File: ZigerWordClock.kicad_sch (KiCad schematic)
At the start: 61 parts, among them J1 SAO 1.69bis, U1 BH1750, U10 BTF-5V-060L-B_SK9822_LED_Stri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, U11 BTF-5V-060L-B_SK9822_LED_Stri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, U12 BTF-5V-060L-B_SK9822_LED_Stri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, U13 BTF-5V-060L-B_SK9822_LED_Stri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, U14 BTF-5V-060L-B_SK9822_LED_Stri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, U15 BTF-5V-060L-B_SK9822_LED_Stri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, U16 BTF-5V-060L-B_SK9822_LED_Stri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, U17 BTF-5V-060L-B_SK9822_LED_Stri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, U18 BTF-5V-060L-B_SK9822_LED_Stri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, U19 BTF-5V-060L-B_SK9822_LED_Stri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, U2 LILYGO(R)_TTGO_T8_ESP32-S2_V1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, U20 IR-Module_38KHz, U3 BTF-5V-060L-B_SK9822_LED_Stri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, U4 LevelShifter, U5 BTF-5V-060L-B_SK9822_LED_Stri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, U6 BTF-5V-060L-B_SK9822_LED_Stri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, U7 BTF-5V-060L-B_SK9822_LED_Stri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, U8 BTF-5V-060L-B_SK9822_LED_Stri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, U9 BTF-5V-060L-B_SK9822_LED_Stri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

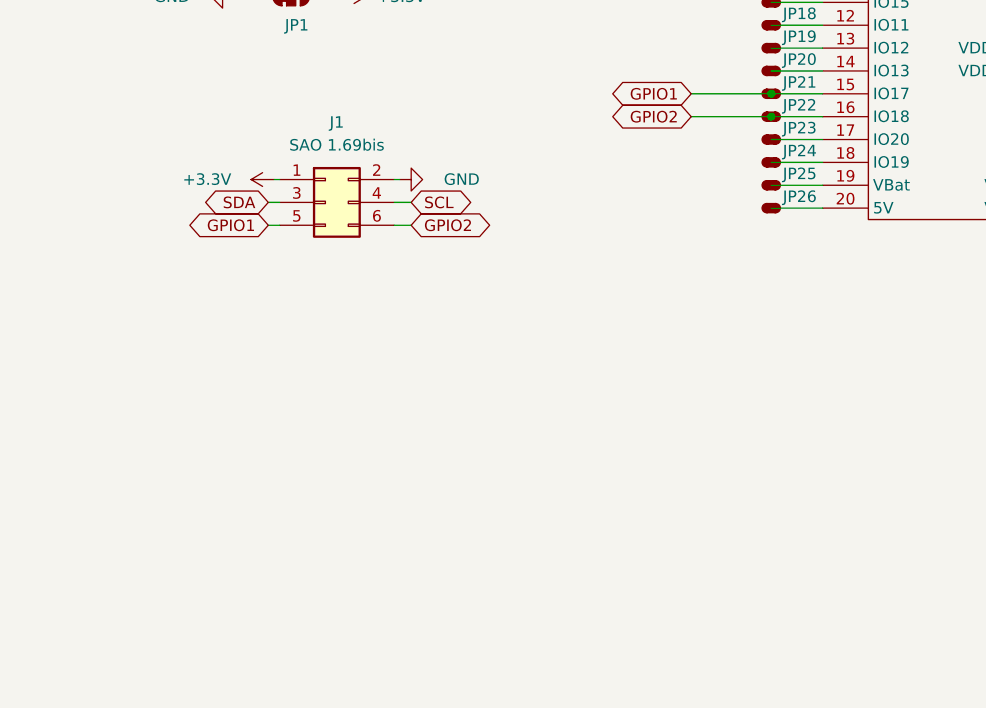
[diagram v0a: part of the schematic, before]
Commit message: Pin labels added
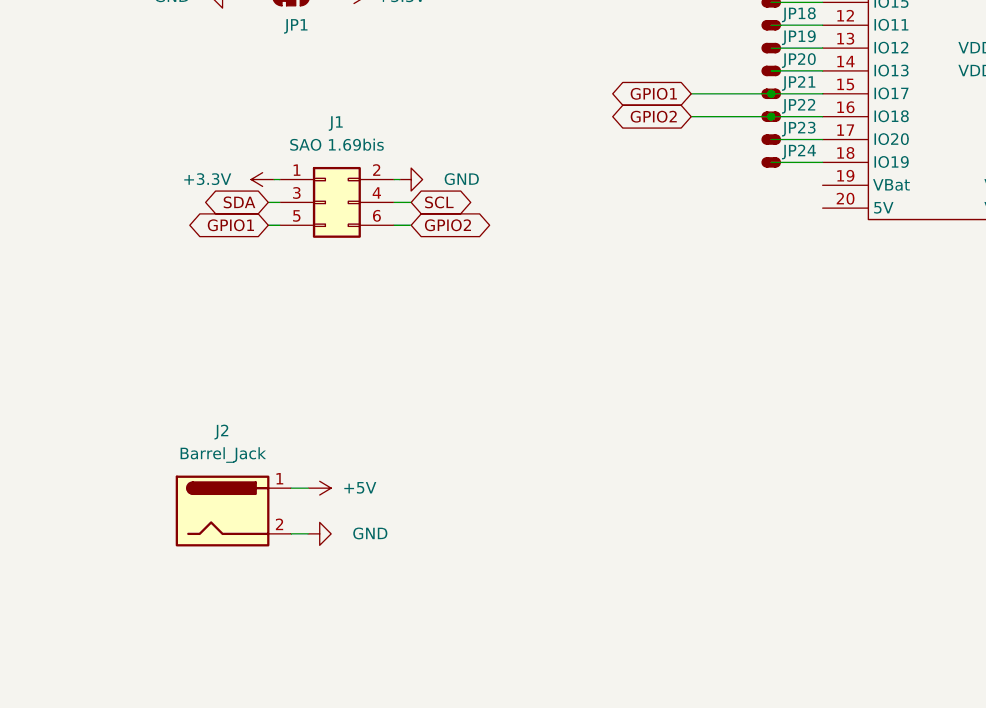
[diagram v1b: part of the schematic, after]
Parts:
- removed JP25, JP26: Pad, WordClock Footprint Library:Pad, symbol WordClock Symbol Library:Pad
- added J2: Barrel_Jack, Connector_PinHeader_2.54mm:PinHeader_1x02_P2.54mm_Vertical, symbol Connector:Barrel_Jack
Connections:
- net +5V: now also J2.1
- net GND: now also J2.2
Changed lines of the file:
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@@
     (stroke (width 0) (type default) (color 0 0 0 0))
   )
-  (wire (pts (xy 154.305 125.095) (xy 160.02 125.095))
-    (stroke (width 0) (type default) (color 0 0 0 0))
-  )
   (wire (pts (xy 165.1 203.2) (xy 168.91 203.2))
     (stroke (width 0) (type default) (color 0 0 0 0))
@@
     (stroke (width 0) (type default) (color 0 0 0 0))
   )
+  (wire (pts (xy 102.87 163.83) (xy 100.965 163.83))
+    (stroke (width 0) (type default) (color 0 0 0 0))
+  )
   (wire (pts (xy 322.58 190.5) (xy 331.47 190.5))
     (stroke (width 0) (type default) (color 0 0 0 0))
@@
     (stroke (width 0) (type default) (color 0 0 0 0))
   )
+  (wire (pts (xy 102.87 158.75) (xy 100.965 158.75))
+    (stroke (width 0) (type default) (color 0 0 0 0))
+  )
   (wire (pts (xy 154.305 112.395) (xy 160.02 112.395))
     (stroke (width 0) (type default) (color 0 0 0 0))
@@
     (stroke (width 0) (type default) (color 0 0 0 0))
   )
-  (wire (pts (xy 154.305 127.635) (xy 160.02 127.635))
-    (stroke (width 0) (type default) (color 0 0 0 0))
-  )
   (wire (pts (xy 320.04 193.04) (xy 331.47 193.04))
     (stroke (width 0) (type default) (color 0 0 0 0))
@@
   (symbol (lib_id "power:GND") (at 189.23 114.935 90) (mirror x) (unit 1)
     (in_bom yes) (on_board yes) (fields_autoplaced)
-    (property "Reference" "#PWR?" (id 0) (at 195.58 114.935 0)
+    (property "Reference" "#PWR0185" (id 0) (at 195.58 114.935 0)
       (effects (font (size 1.27 1.27)) hide)
     )
@@
     (pin "GND_2")
   )
+  (symbol (lib_id "Connector:Barrel_Jack") (at 93.345 161.29 0) (unit 1)
+    (in_bom yes) (on_board yes) (fields_autoplaced)
+    (property "Reference" "J2" (id 0) (at 93.345 152.4 0))
+    (property "Value" "Barrel_Jack" (id 1) (at 93.345 154.94 0))
+    (property "Footprint" "Connector_PinHeader_2.54mm:PinHeader_1x02_P2.54mm_Vertical" (id 2) (at 94.615 162.306 0)
+      (effects (font (size 1.27 1.27)) hide)
+    )
+    (property "Datasheet" "~" (id 3) (at 94.615 162.306 0)
+      (effects (font (size 1.27 1.27)) hide)
+    )
+    (pin "1")
+    (pin "2")
+  )
   (symbol (lib_id "power:+5V") (at 331.47 73.66 90) (unit 1)
     (in_bom yes) (on_board yes) (fields_autoplaced)
@@
     (pin "1")
   )
+  (symbol (lib_id "power:GND") (at 102.87 163.83 90) (unit 1)
+    (in_bom yes) (on_board yes)
+    (property "Reference" "#PWR0183" (id 0) (at 109.22 163.83 0)
+      (effects (font (size 1.27 1.27)) hide)
+    )
+    (property "Value" "GND" (id 1) (at 111.76 163.83 90)
+      (effects (font (size 1.27 1.27)) (justify left))
+    )
+    (property "Footprint" "" (id 2) (at 102.87 163.83 0)
+      (effects (font (size 1.27 1.27)) hide)
+    )
+    (property "Datasheet" "" (id 3) (at 102.87 163.83 0)
+      (effects (font (size 1.27 1.27)) hide)
+    )
+    (pin "1")
+  )
   (symbol (lib_id "power:GND") (at 113.03 124.46 90) (unit 1)
     (in_bom yes) (on_board yes)
@@
     (pin "1")
   )
-  (symbol (lib_id "WordClock Symbol Library:Pad") (at 154.305 125.095 0) (unit 1)
-    (in_bom yes) (on_board yes)
-    (property "Reference" "JP25" (id 0) (at 157.48 123.825 0))
-    (property "Value" "Pad" (id 1) (at 154.305 126.619 0)
-      (effects (font (size 1.27 1.27)) hide)
-    )
-    (property "Footprint" "WordClock Footprint Library:Pad" (id 2) (at 154.305 125.095 0)
-      (effects (font (size 1.27 1.27)) hide)
-    )
-    (property "Datasheet" "" (id 3) (at 154.305 125.095 0)
-      (effects (font (size 1.27 1.27)) hide)
-    )
-    (pin "1")
-  )
   (symbol (lib_id "WordClock Symbol Library:BTF-5V-060L-B_SK9822_LED_Strip_-_11_LED") (at 355.6 185.42 0) (unit 1)
     (in_bom yes) (on_board yes)
@@
     (pin "1")
   )
-  (symbol (lib_id "WordClock Symbol Library:Pad") (at 154.305 127.635 0) (unit 1)
-    (in_bom yes) (on_board yes)
-    (property "Reference" "JP26" (id 0) (at 157.48 126.365 0))
-    (property "Value" "Pad" (id 1) (at 154.305 129.159 0)
-      (effects (font (size 1.27 1.27)) hide)
-    )
-    (property "Footprint" "WordClock Footprint Library:Pad" (id 2) (at 154.305 127.635 0)
-      (effects (font (size 1.27 1.27)) hide)
-    )
-    (property "Datasheet" "" (id 3) (at 154.305 127.635 0)
-      (effects (font (size 1.27 1.27)) hide)
-    )
-    (pin "1")
-  )
   (symbol (lib_id "WordClock Symbol Library:Pad") (at 193.675 99.695 0) (mirror y) (unit 1)
     (in_bom yes) (on_board yes)
@@
     (pin "1")
   )
+  (symbol (lib_id "power:+5V") (at 102.87 158.75 270) (unit 1)
+    (in_bom yes) (on_board yes)
+    (property "Reference" "#PWR0184" (id 0) (at 99.06 158.75 0)
+      (effects (font (size 1.27 1.27)) hide)
+    )
+    (property "Value" "+5V" (id 1) (at 106.68 158.75 90)
+      (effects (font (size 1.27 1.27)) (justify left))
+    )
+    (property "Footprint" "" (id 2) (at 102.87 158.75 0)
+      (effects (font (size 1.27 1.27)) hide)
+    )
+    (property "Datasheet" "" (id 3) (at 102.87 158.75 0)
+      (effects (font (size 1.27 1.27)) hide)
+    )
+    (pin "1")
+  )
   (sheet_instances
     (path "/" (page "1"))
@@
       (reference "#PWR0182") (unit 1) (value "GND") (footprint "")
     )
+    (path "/90dc646b-1260-4819-b979-749c6156871c"
+      (reference "#PWR0183") (unit 1) (value "GND") (footprint "")
+    )
+    (path "/ff5014df-9c36-4298-a3cd-1c6d9438fdcc"
+      (reference "#PWR0184") (unit 1) (value "+5V") (footprint "")
+    )
     (path "/563b46d5-a373-458f-a4c2-52a3d13e4af7"
-      (reference "#PWR?") (unit 1) (value "GND") (footprint "")
+      (reference "#PWR0185") (unit 1) (value "GND") (footprint "")
     )
     (path "/5c8239f8-fd73-4510-a108-c250e3567c1c"
       (reference "J1") (unit 1) (value "SAO 1.69bis") (footprint "Connector_PinSocket_2.54mm:PinSocket_2x03_P2.54mm_Vertical_SMD")
     )
+    (path "/896391fa-77aa-4617-be63-4c92c9128a73"
+      (reference "J2") (unit 1) (value "Barrel_Jack") (footprint "Connector_PinHeader_2.54mm:PinHeader_1x02_P2.54mm_Vertical")
+    )
     (path "/a52bba10-7ae9-4aa5-9658-4b8c2b27a0a3"
       (reference "JP1") (unit 1) (value "SolderJumper_3_Bridged12") (footprint "Jumper:SolderJumper-3_P1.3mm_Bridged12_RoundedPad1.0x1.5mm_NumberLabels")
@@
       (reference "JP24") (unit 1) (value "Pad") (footprint "WordClock Footprint Library:Pad")
     )
-    (path "/b0d7f0aa-87d5-44ca-acae-4215827172e9"
-      (reference "JP25") (unit 1) (value "Pad") (footprint "WordClock Footprint Library:Pad")
-    )
-    (path "/ef49b3eb-a83c-4ca8-8b1b-f5fb922aaae1"
-      (reference "JP26") (unit 1) (value "Pad") (footprint "WordClock Footprint Library:Pad")
-    )
     (path "/c090f64b-266f-4a5a-bc6d-21cef94d0628"

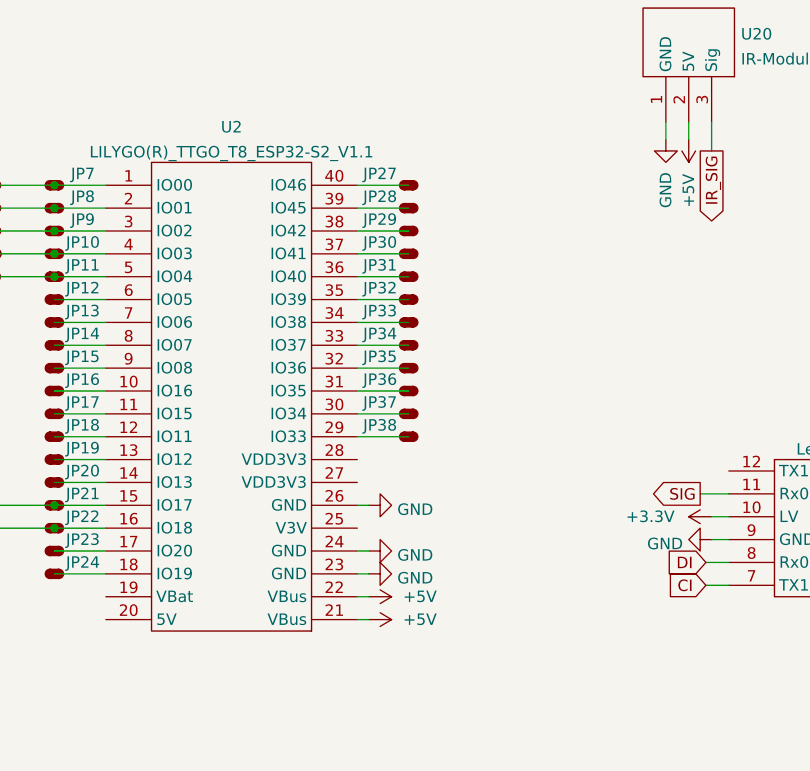
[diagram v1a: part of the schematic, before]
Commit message: compabiliy with the display ESP32 module
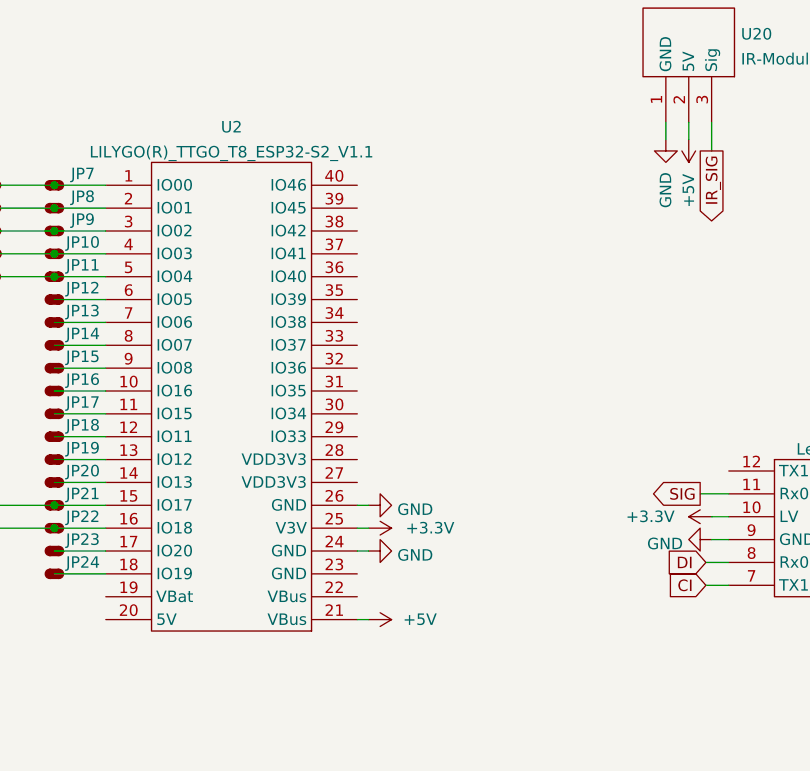
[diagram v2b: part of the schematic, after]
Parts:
- removed JP27, JP28, JP29, JP30, JP31, JP32, JP33, JP34, JP35, JP36, JP37, JP38: Pad, WordClock Footprint Library:Pad, symbol WordClock Symbol Library:Pad
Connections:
- net +3V3: now also U2.25 (V3V)
- net +5V: no longer U2.22 (VBus)
- net GND: no longer U2.23 (GND)
